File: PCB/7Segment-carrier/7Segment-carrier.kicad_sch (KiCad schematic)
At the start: 2 parts, among them J1 PPTC101LFBN-RC

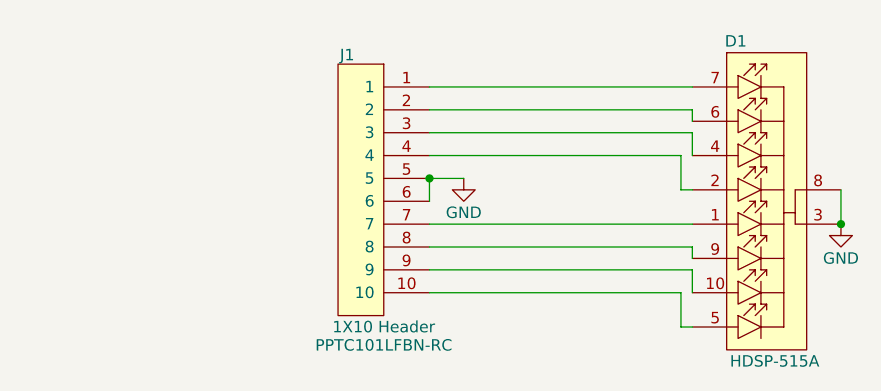
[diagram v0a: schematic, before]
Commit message: All Hardware Tweaked / 3D Renders
PCBs for Actuator Control, Recline Control HID, and 7 Segment carrier are all complete with full 3D models rendering. 3D Renders of all board added to repository img directory.
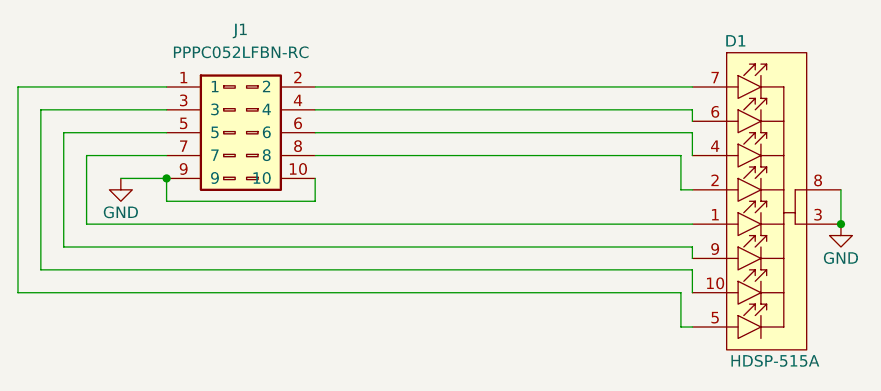
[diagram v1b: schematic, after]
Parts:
- removed J1: PPTC101LFBN-RC, AVR-KiCAD-Lib-Connectors:Female_Header_Straight_1x10_Pitch2.54mm, symbol AVR-KiCAD-Lib-Connectors:PPTC101LFBN-RC
- added J1: PPPC052LFBN-RC, AVR-KiCAD-Lib-Connectors:PPPC052LFBN-RC_2x05_Pitch2.54mm, symbol AVR-KiCAD-Lib-Connectors:PPPC052LFBN-RC
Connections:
- net GND: now also J1.10, J1.9
- net at D1.1: now also J1.7
- net at D1.10: now also J1.3
- net at D1.2: now also J1.8
- net at D1.4: now also J1.6
- net at D1.5: now also J1.1
- net at D1.6: now also J1.4
- net at D1.7: now also J1.2
- net at D1.9: now also J1.5
